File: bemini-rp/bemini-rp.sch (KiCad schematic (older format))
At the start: 66 parts, among them J1 USB_C_Receptacle_USB2.0, K1 MX-NoLED, K10 MX-NoLED, K11 MX-NoLED, K12 MX-NoLED, K13 MX-NoLED, K2 MX-NoLED, K3 MX-NoLED, K4 MX-NoLED, K5 MX-NoLED, K6 MX-NoLED, K7 MX-NoLED, K8 MX-NoLED, K9 MX-NoLED, Q1 BSS138, SW1 BOOT, SW2 RESET, U1 RP2040, U2 W25Q128JV, U3 AP2112K-3.3, Y1 12MHz

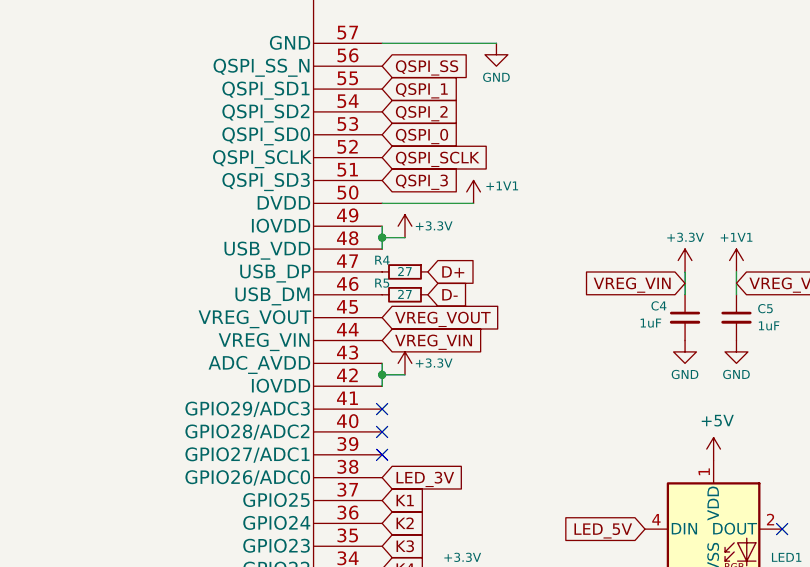
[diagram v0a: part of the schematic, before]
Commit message: update usb resistors
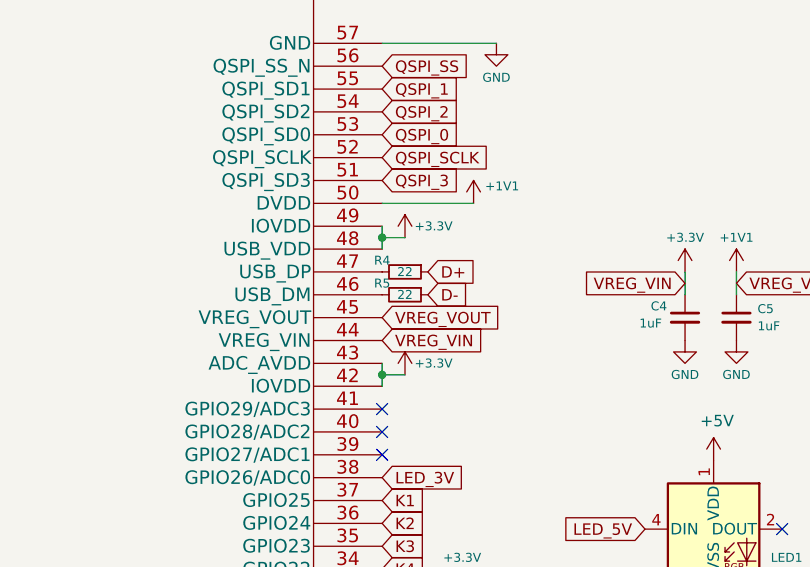
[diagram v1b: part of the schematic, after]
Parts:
- R4, R5: value 27 -> 22
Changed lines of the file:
@@
 D+
-$Comp
-L Device:R_Small R4
-U 1 1 60976113
-P 7800 2200
-F 0 "R4" V 7750 2100 39  0000 C CNN
-F 1 "27" V 7800 2200 39  0000 C CNN
-F 2 "Keebio-Parts:R_0402" H 7800 2200 50  0001 C CNN
-F 3 "~" H 7800 2200 50  0001 C CNN
-	1    7800 2200
-	0    1    1    0
-$EndComp
 $Comp
 L Device:R_Small R5
@@
 P 7800 2300
 F 0 "R5" V 7750 2200 39  0000 C CNN
-F 1 "27" V 7800 2300 39  0000 C CNN
+F 1 "22" V 7800 2300 39  0000 C CNN
 F 2 "Keebio-Parts:R_0402" H 7800 2300 50  0001 C CNN
 F 3 "~" H 7800 2300 50  0001 C CNN
@@
 	0    1    1    0
 $EndComp
+$Comp
+L Device:R_Small R4
+U 1 1 60976113
+P 7800 2200
+F 0 "R4" V 7750 2100 39  0000 C CNN
+F 1 "22" V 7800 2200 39  0000 C CNN
+F 2 "Keebio-Parts:R_0402" H 7800 2200 50  0001 C CNN
+F 3 "~" H 7800 2200 50  0001 C CNN
+	1    7800 2200
+	0    1    1    0
+$EndComp
